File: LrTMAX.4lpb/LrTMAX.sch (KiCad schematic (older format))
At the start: 122 parts, among them J1 USB_B_Micro, J2 SM06B-SRSS-TB, Q1 2N7002, SW1 Tact_SW_8mm, SW10 EC11_SMD, SW11 EC11_SMD, SW12 EC11_SMD, SW13 EC11_SMD, SW14 EC11_SMD, SW15 EC11_SMD, SW16 EC11_SMD, SW17 EC11_SMD, SW2 Tact_SW_8mm, SW3 Tact_SW_8mm, SW4 Tact_SW_8mm, SW5 Tact_SW_8mm, SW6 Tact_SW_8mm, SW7 Tact_SW_8mm, SW8 Tact_SW_8mm, U1 STM32F072C8Tx, U3 SSD1306_OLED_0.91, U4 SPX3819M5-L3-3TR

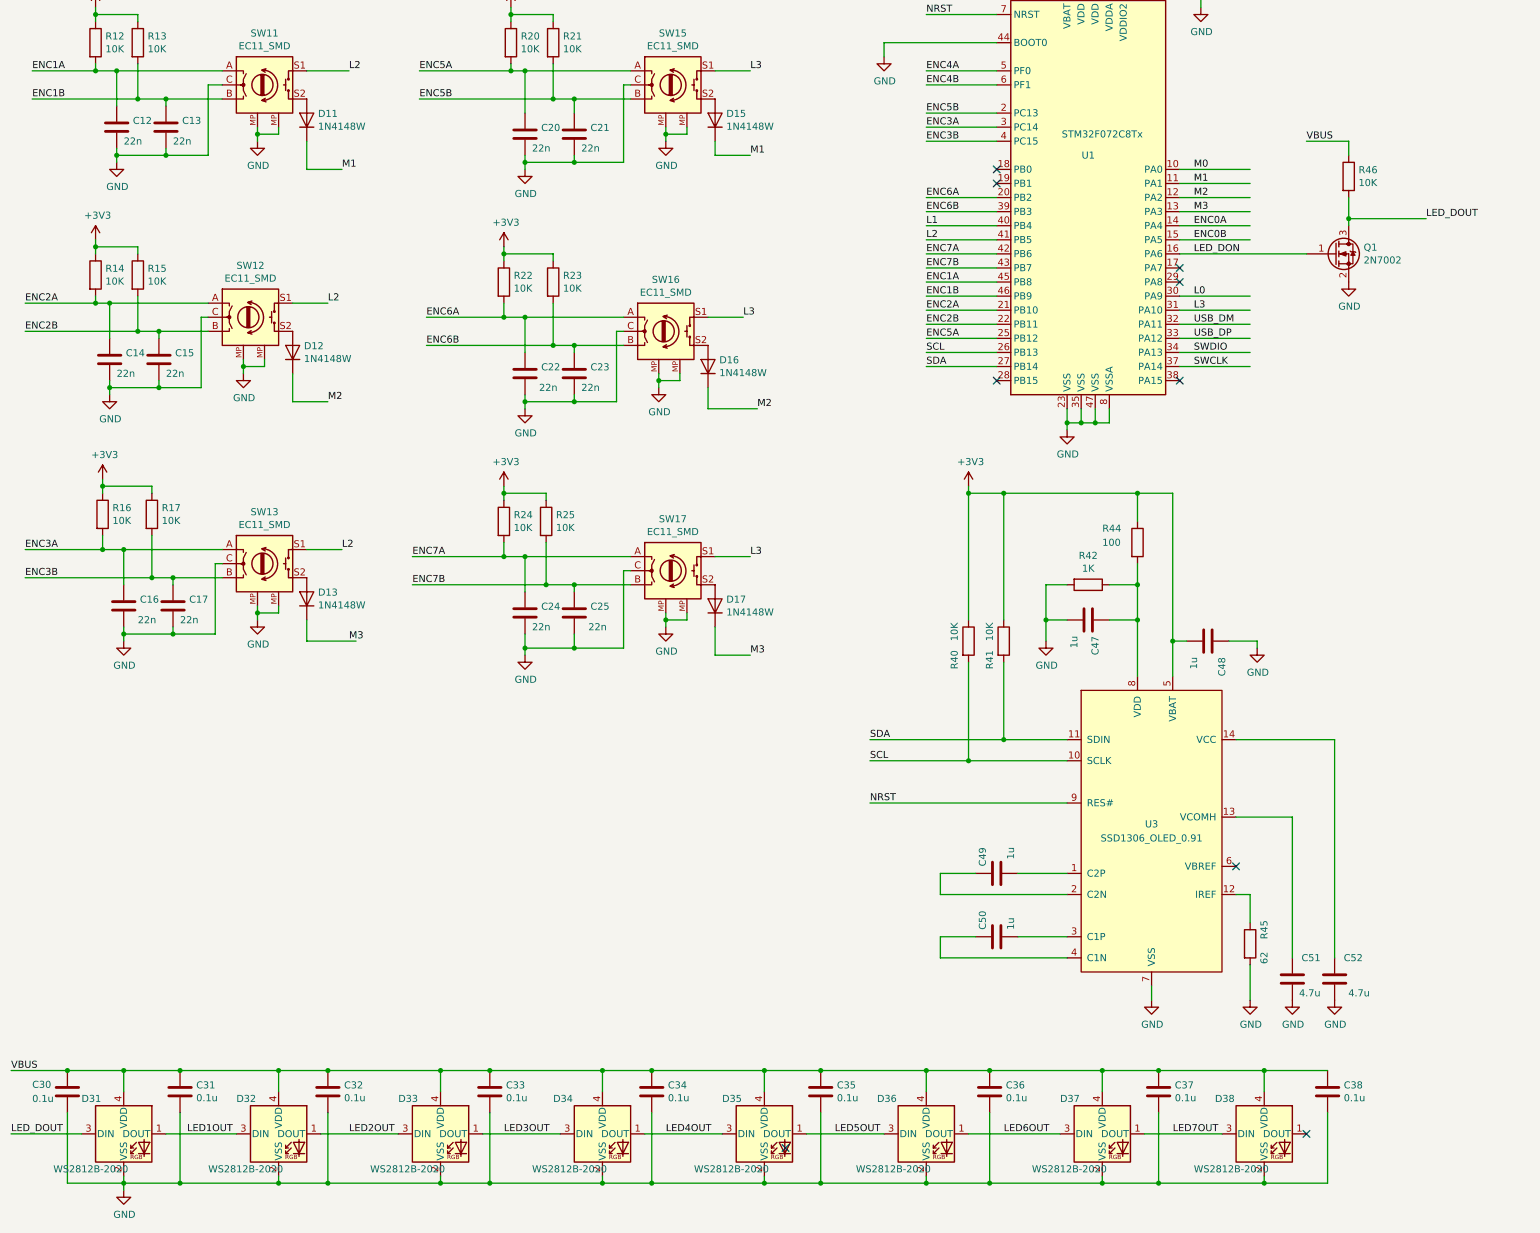
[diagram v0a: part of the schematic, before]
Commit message: 0.46-3
Adjust LED PWM width to meed WS2812-2020 spec.
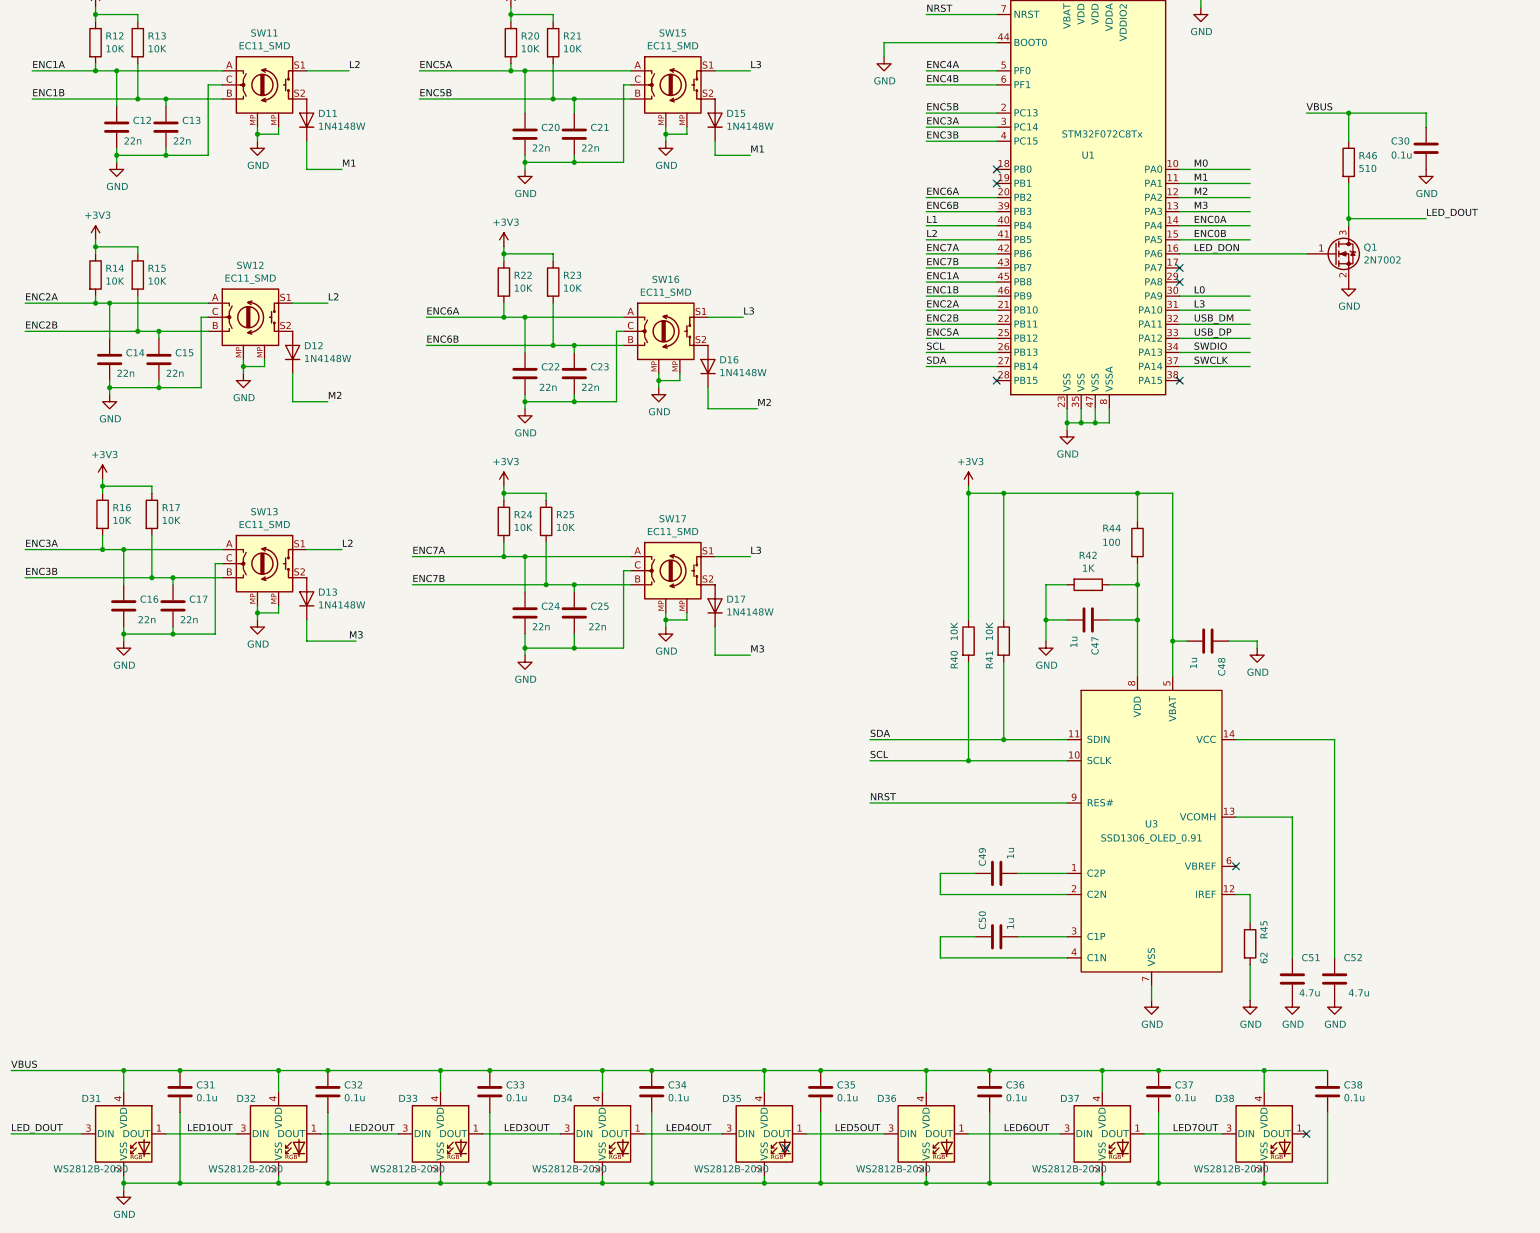
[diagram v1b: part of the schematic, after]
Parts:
- R46: value 10K -> 510
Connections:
- wire segments 497 -> 496
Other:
- moved on the sheet: C30, R46
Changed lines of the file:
@@
 	1600 10300 1600 10150
 Connection ~ 1600 10150
-Wire Wire Line
-	1600 10150 1200 10150
 Text Label 800  10150 0    50   ~ 0
 VBUS
@@
 L LrE-6-rescue:R-Device R46
 U 1 1 5D024220
-P 10300 3800
-F 0 "R46" H 10370 3846 50  0000 L CNN
-F 1 "10K" H 10370 3755 50  0000 L CNN
-F 2 "Resistor_SMD:R_0805_2012Metric" V 10230 3800 50  0001 C CNN
-F 3 "~" H 10300 3800 50  0001 C CNN
-	1    10300 3800
+P 10300 3700
+F 0 "R46" H 10370 3746 50  0000 L CNN
+F 1 "510" H 10370 3655 50  0000 L CNN
+F 2 "Resistor_SMD:R_0805_2012Metric" V 10230 3700 50  0001 C CNN
+F 3 "~" H 10300 3700 50  0001 C CNN
+	1    10300 3700
 	1    0    0    -1
 $EndComp
@@
 	10300 4150 10300 4100
 Wire Wire Line
-	10000 3550 10300 3550
-Wire Wire Line
-	10300 3550 10300 3650
+	10300 3350 10300 3550
 Wire Wire Line
 	10300 4100 10850 4100
 Connection ~ 10300 4100
 Wire Wire Line
-	10300 4100 10300 3950
+	10300 4100 10300 3850
 Text Label 9200 4350 0    50   ~ 0
 LED_DON
-Text Label 10000 3550 0    50   ~ 0
+Text Label 10000 3350 0    50   ~ 0
 VBUS
 $Comp
 L LrE-6-rescue:C-Device C30
 U 1 1 5D54B231
-P 1200 10300
-F 0 "C30" H 950 10350 50  0000 L CNN
-F 1 "0.1u" H 950 10250 50  0000 L CNN
-F 2 "Capacitor_SMD:C_0805_2012Metric" H 1238 10150 50  0001 C CNN
-F 3 "~" H 1200 10300 50  0001 C CNN
-	1    1200 10300
-	1    0    0    -1
-$EndComp
-Connection ~ 1200 10150
-Wire Wire Line
-	1600 10950 1200 10950
-Wire Wire Line
-	1200 10950 1200 10450
+P 10850 3600
+F 0 "C30" H 10600 3650 50  0000 L CNN
+F 1 "0.1u" H 10600 3550 50  0000 L CNN
+F 2 "Capacitor_SMD:C_0805_2012Metric" H 10888 3450 50  0001 C CNN
+F 3 "~" H 10850 3600 50  0001 C CNN
+	1    10850 3600
+	1    0    0    -1
+$EndComp
 Wire Wire Line
 	800  10600 1300 10600
-Wire Wire Line
-	800  10150 1200 10150
 Wire Wire Line
 	9100 4350 10000 4350
@@
 Wire Wire Line
 	5800 3650 6050 3650
+Wire Wire Line
+	800  10150 1600 10150
+$Comp
+L LrE-6-rescue:GND-power #PWR?
+U 1 1 60DE7033
+P 10850 3750
+F 0 "#PWR?" H 10850 3500 50  0001 C CNN
+F 1 "GND" H 10855 3577 50  0000 C CNN
+F 2 "" H 10850 3750 50  0001 C CNN
+F 3 "" H 10850 3750 50  0001 C CNN
+	1    10850 3750
+	1    0    0    -1
+$EndComp
+Wire Wire Line
+	10300 3350 10850 3350
+Wire Wire Line
+	10850 3350 10850 3450
+Connection ~ 10300 3350
+Wire Wire Line
+	10000 3350 10300 3350
 $EndSCHEMATC

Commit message: 0.47-5
some Debug tweak.
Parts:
- R46: value 510 -> 1.2K
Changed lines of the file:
@@
 P 10300 3700
 F 0 "R46" H 10370 3746 50  0000 L CNN
-F 1 "510" H 10370 3655 50  0000 L CNN
+F 1 "1.2K" H 10370 3655 50  0000 L CNN
 F 2 "Resistor_SMD:R_0805_2012Metric" V 10230 3700 50  0001 C CNN
 F 3 "~" H 10300 3700 50  0001 C CNN

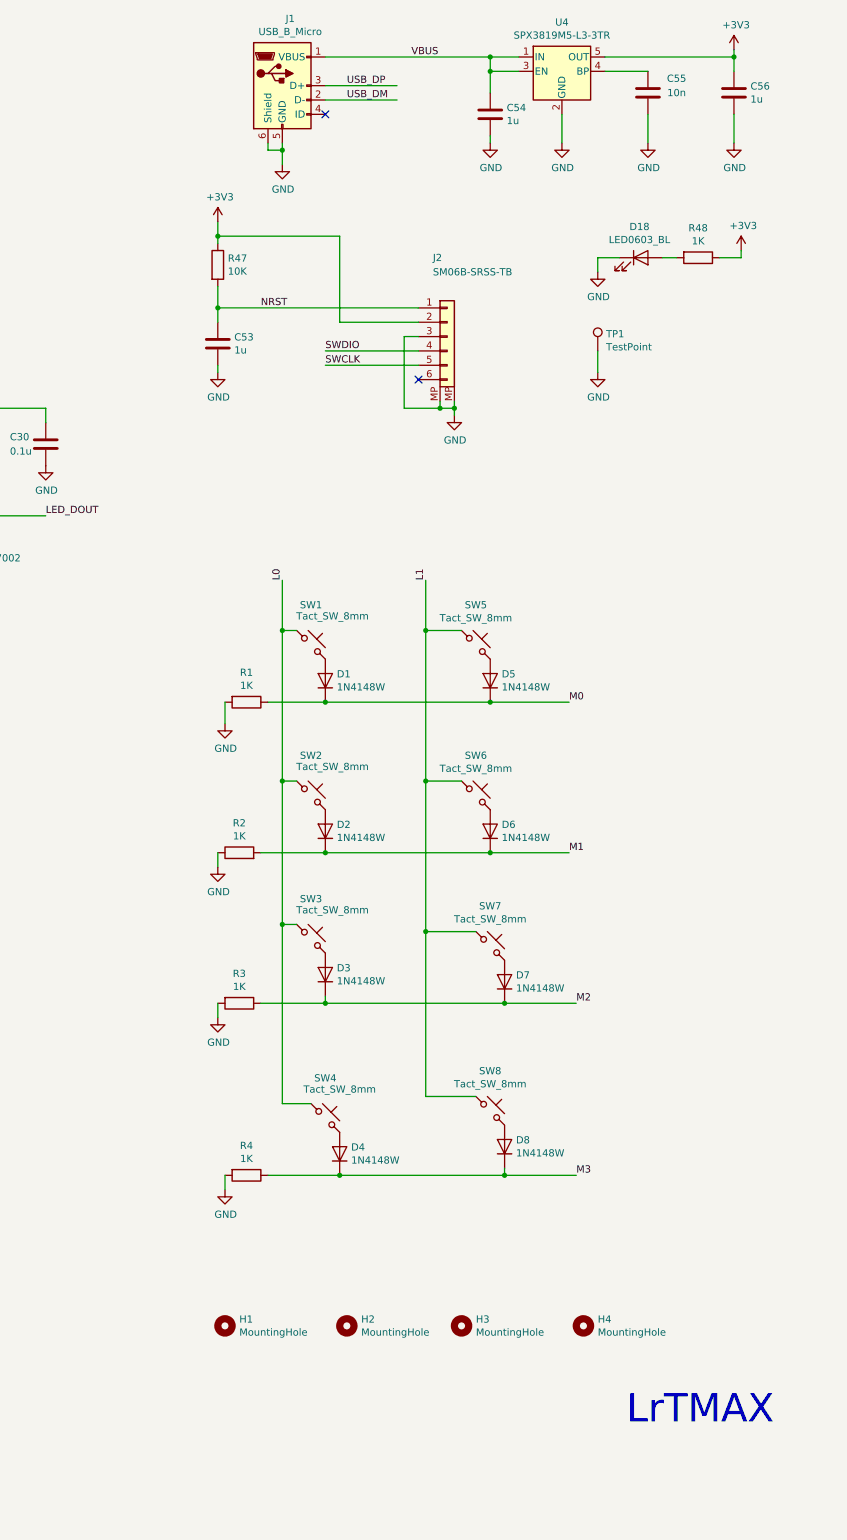
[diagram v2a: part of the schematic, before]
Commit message: 0.49c
USB conn. changed to typeC
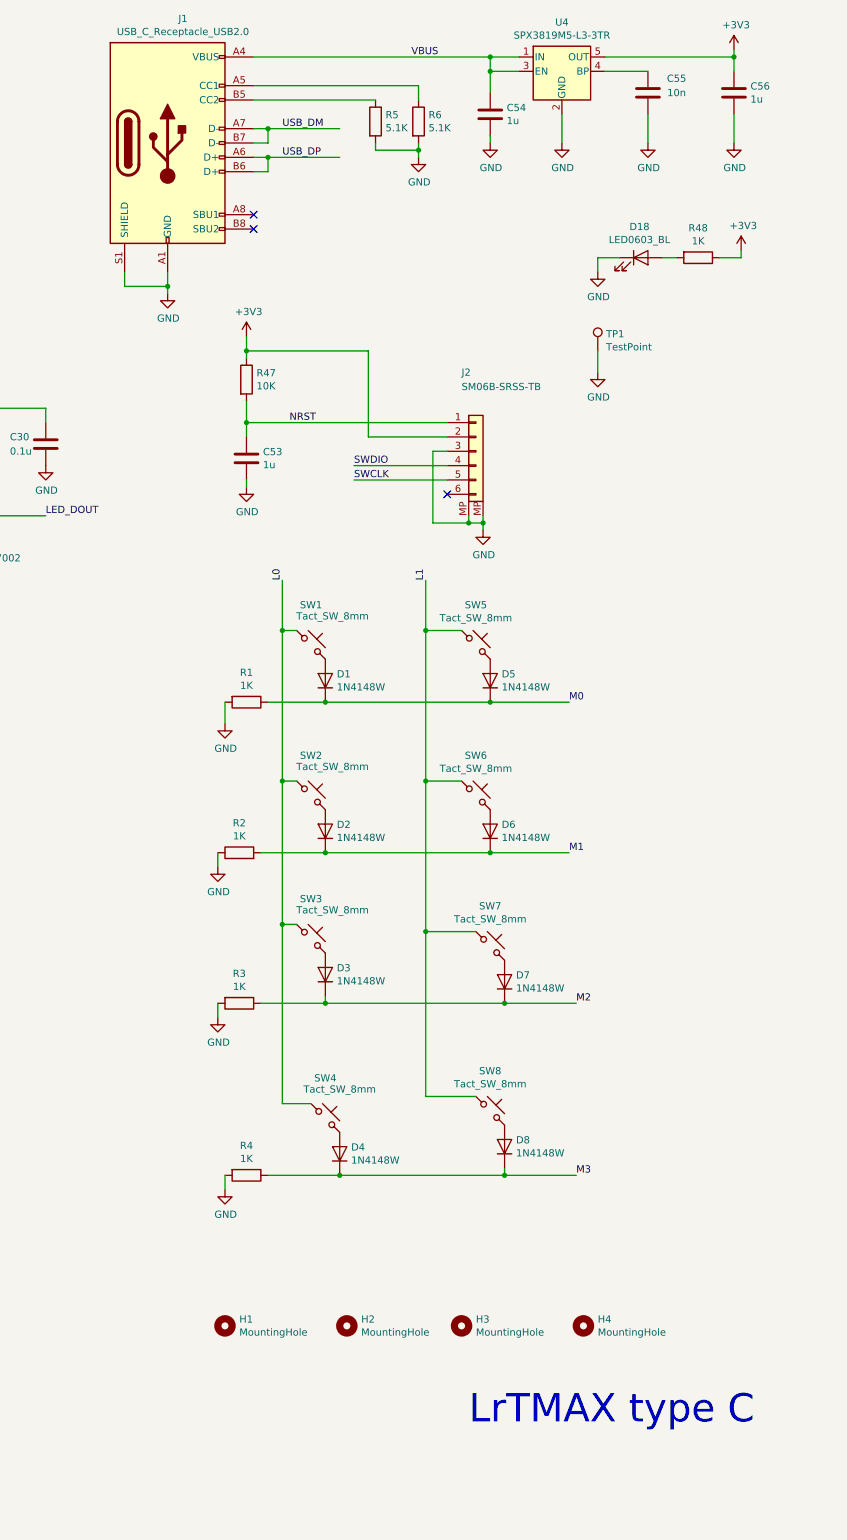
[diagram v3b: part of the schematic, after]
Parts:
- removed J1: USB_B_Micro, LrE-6:USB_Micro-B_MCUBF-09_1, symbol LrE-6-rescue:USB_B_Micro-Connector
- added J1: USB_C_Receptacle_USB2.0, Connector_USB:USB_C_Receptacle_HRO_TYPE-C-31-M-12, symbol LrE-6:USB_C_Receptacle_USB2.0
- added R5, R6: 5.1K, Resistor_SMD:R_0805_2012Metric, symbol LrE-6-rescue:R-Device
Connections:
- wire segments 496 -> 509
- no-connect marks 11 -> 12
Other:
- note added: "LrTMAX type C"
- note removed: "LrTMAX"
- moved on the sheet: C53, J2, R47

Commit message: 0.49c-3
KiCAD library resrore & ENC5 ISR routine.
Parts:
- R42, R44: symbol Device:R -> LrE-6-rescue:R-Device
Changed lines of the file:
@@
 	7600 6950 7600 6050
 $Comp
-L Device:R R44
+L LrE-6-rescue:R-Device R44
 U 1 1 5EEE6BD3
 P 8800 6400
@@
 $EndComp
 $Comp
-L Device:R R42
+L LrE-6-rescue:R-Device R42
 U 1 1 5EEE73A1
 P 8450 6700
